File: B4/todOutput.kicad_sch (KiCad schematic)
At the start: 0 parts

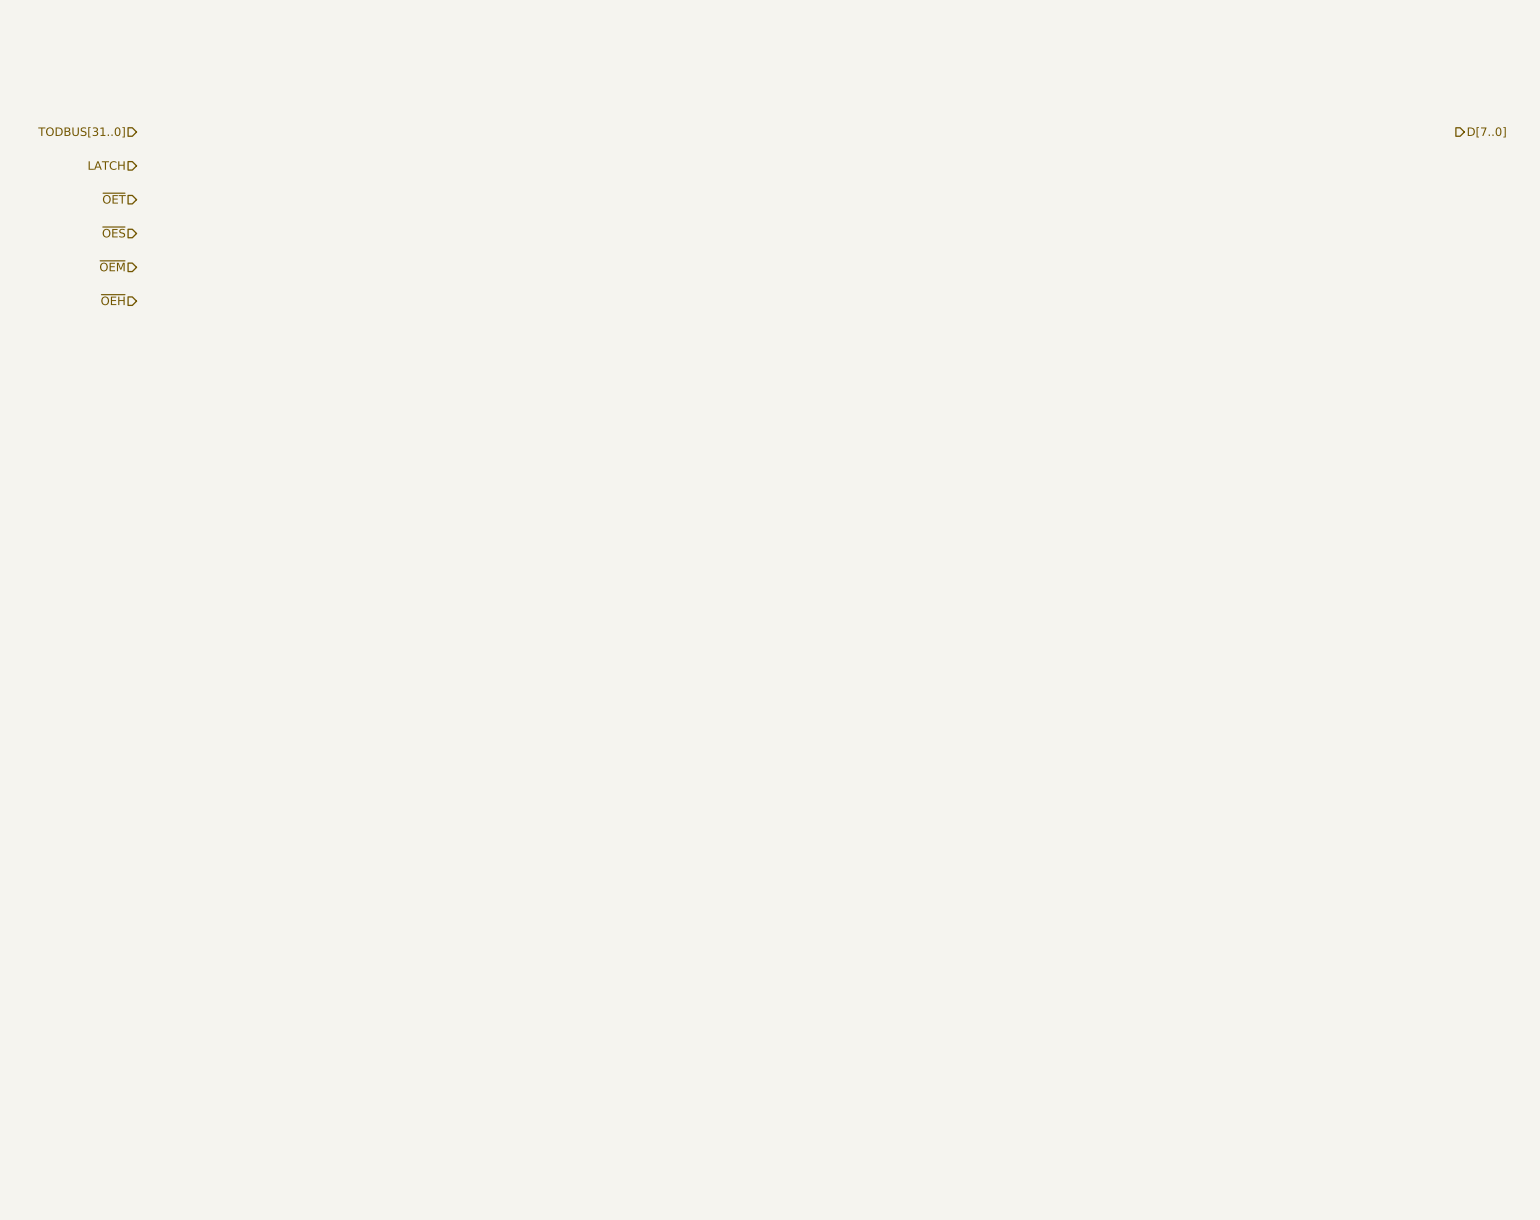
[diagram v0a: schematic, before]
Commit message: B2 refactored. B4 Added. TOD sch completed.
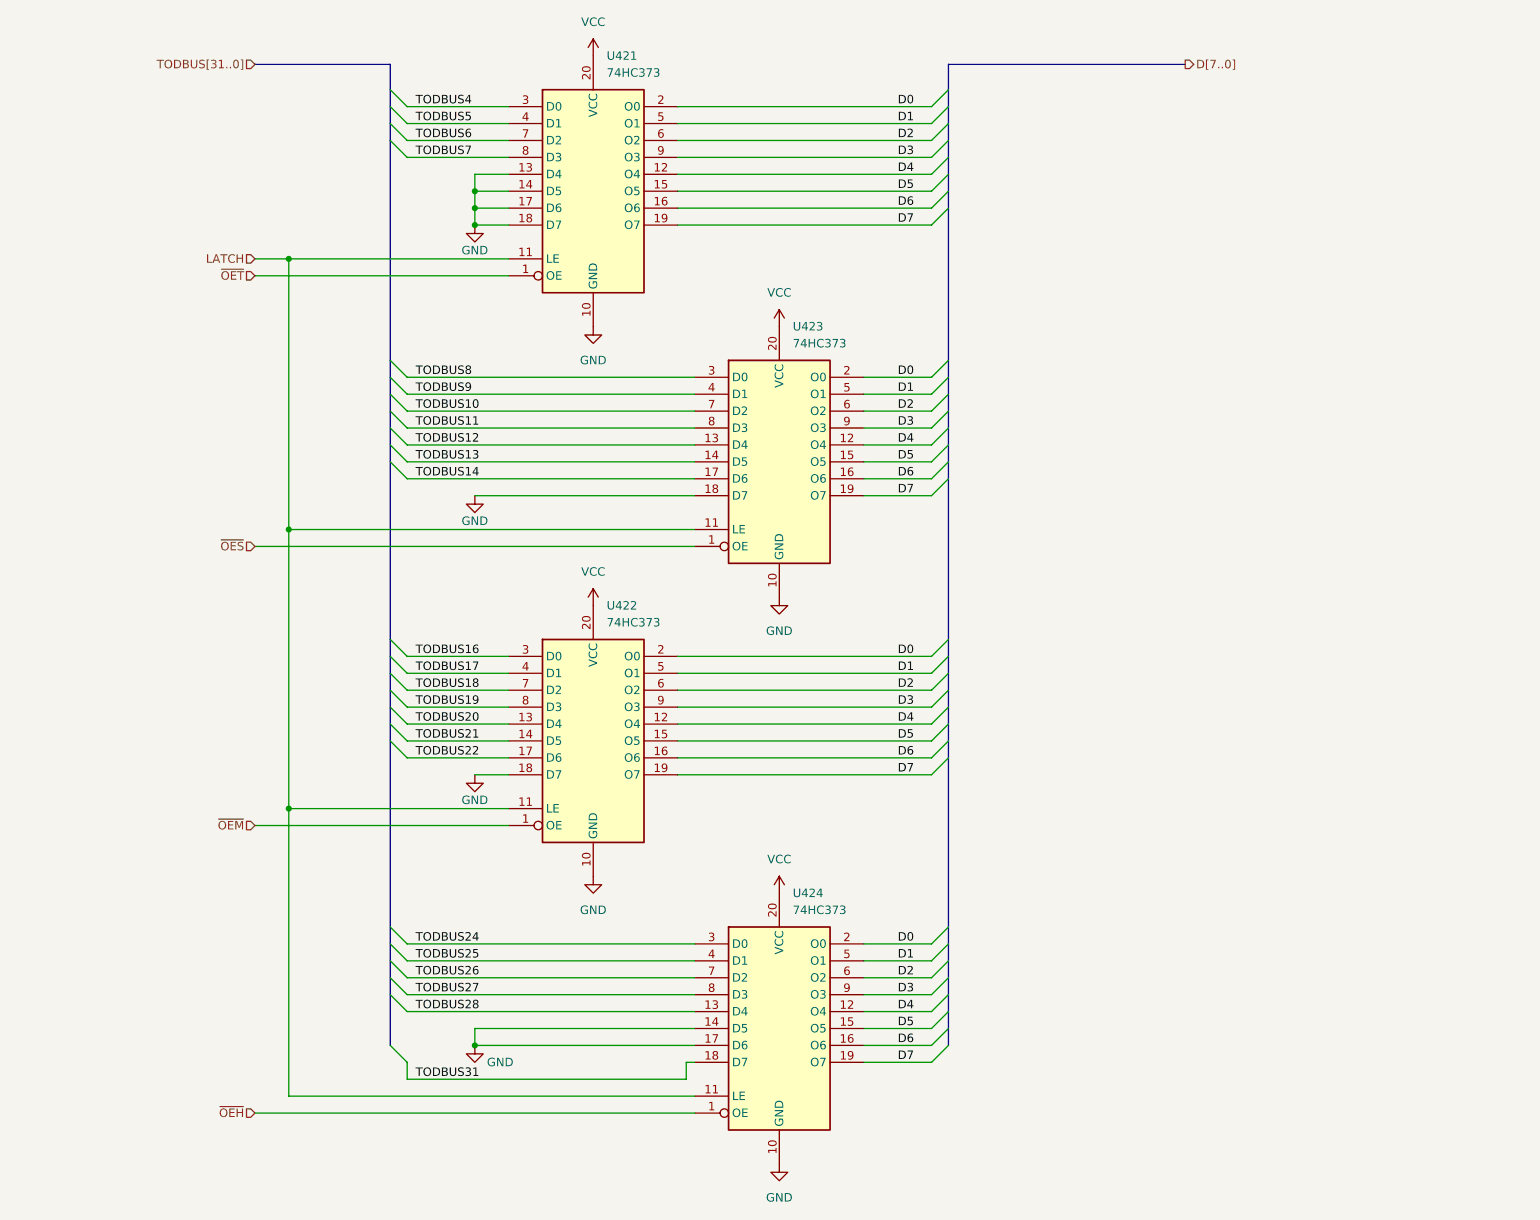
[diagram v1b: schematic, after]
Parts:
- added U421, U422, U423, U424: 74HC373, Package_SO:SOIC-20W_7.5x12.8mm_P1.27mm, symbol 74xx:74HC373
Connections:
- net LATCH: now also U421.11 (LE), U422.11 (LE), U423.11 (LE), U424.11 (LE)
- net ~{OEH}: now also U424.1 (OE)
- net ~{OEM}: now also U422.1 (OE)
- net ~{OES}: now also U423.1 (OE)
- net ~{OET}: now also U421.1 (OE)
- new net D0: U421.2 (O0), U422.2 (O0), U423.2 (O0), U424.2 (O0)
- new net D1: U421.5 (O1), U422.5 (O1), U423.5 (O1), U424.5 (O1)
- new net D2: U421.6 (O2), U422.6 (O2), U423.6 (O2), U424.6 (O2)
- new net D3: U421.9 (O3), U422.9 (O3), U423.9 (O3), U424.9 (O3)
- new net D4: U421.12 (O4), U422.12 (O4), U423.12 (O4), U424.12 (O4)
- new net D5: U421.15 (O5), U422.15 (O5), U423.15 (O5), U424.15 (O5)
- new net D6: U421.16 (O6), U422.16 (O6), U423.16 (O6), U424.16 (O6)
- new net D7: U421.19 (O7), U422.19 (O7), U423.19 (O7), U424.19 (O7)
- new net GND: U421.10 (GND), U421.13 (D4), U421.14 (D5), U421.17 (D6), U421.18 (D7), U422.10 (GND), U422.18 (D7), U423.10 (GND), U423.18 (D7), U424.10 (GND), U424.14 (D5), U424.17 (D6)
- new net TODBUS10: U423.7 (D2)
- new net TODBUS11: U423.8 (D3)
- new net TODBUS12: U423.13 (D4)
- new net TODBUS13: U423.14 (D5)
- new net TODBUS14: U423.17 (D6)
- new net TODBUS16: U422.3 (D0)
- new net TODBUS17: U422.4 (D1)
- new net TODBUS18: U422.7 (D2)
- new net TODBUS19: U422.8 (D3)
- new net TODBUS20: U422.13 (D4)
- new net TODBUS21: U422.14 (D5)
- new net TODBUS22: U422.17 (D6)
- new net TODBUS24: U424.3 (D0)
- new net TODBUS25: U424.4 (D1)
- new net TODBUS26: U424.7 (D2)
- new net TODBUS27: U424.8 (D3)
- new net TODBUS28: U424.13 (D4)
- new net TODBUS31: U424.18 (D7)
- new net TODBUS4: U421.3 (D0)
- new net TODBUS5: U421.4 (D1)
- new net TODBUS6: U421.7 (D2)
- new net TODBUS7: U421.8 (D3)
- new net TODBUS8: U423.3 (D0)
- new net TODBUS9: U423.4 (D1)
- new net VCC: U421.20 (VCC), U422.20 (VCC), U423.20 (VCC), U424.20 (VCC)

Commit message: TOD is here
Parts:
- renumbered U421 to U405
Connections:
- net D0: now also U405.5 (O1), U422.5 (O1), U423.5 (O1), U424.5 (O1); no longer U405.2 (O0), U422.2 (O0), U423.2 (O0), U424.2 (O0)
- net D1: now also U405.2 (O0), U422.2 (O0), U423.2 (O0), U424.2 (O0); no longer U405.5 (O1), U422.5 (O1), U423.5 (O1), U424.5 (O1)
- net D4: now also U405.15 (O5), U422.15 (O5), U423.15 (O5), U424.15 (O5); no longer U405.12 (O4), U422.12 (O4), U423.12 (O4), U424.12 (O4)
- net D5: now also U405.16 (O6), U422.16 (O6), U423.16 (O6), U424.16 (O6); no longer U405.15 (O5), U422.15 (O5), U423.15 (O5), U424.15 (O5)
- net D6: now also U405.12 (O4), U422.12 (O4), U423.12 (O4), U424.12 (O4); no longer U405.16 (O6), U422.16 (O6), U423.16 (O6), U424.16 (O6)
- net GND: now also U424.13 (D4); no longer U424.14 (D5)
- net TODBUS12: now also U423.14 (D5); no longer U423.13 (D4)
- net TODBUS13: now also U423.17 (D6); no longer U423.14 (D5)
- net TODBUS14: now also U423.13 (D4); no longer U423.17 (D6)
- net TODBUS16: now also U422.4 (D1); no longer U422.3 (D0)
- net TODBUS17: now also U422.3 (D0); no longer U422.4 (D1)
- net TODBUS20: now also U422.14 (D5); no longer U422.13 (D4)
- net TODBUS21: now also U422.17 (D6); no longer U422.14 (D5)
- net TODBUS22: now also U422.13 (D4); no longer U422.17 (D6)
- net TODBUS24: now also U424.4 (D1); no longer U424.3 (D0)
- net TODBUS25: now also U424.3 (D0); no longer U424.4 (D1)
- net TODBUS28: now also U424.14 (D5); no longer U424.13 (D4)
- net TODBUS4: now also U405.4 (D1); no longer U405.3 (D0)
- net TODBUS5: now also U405.3 (D0); no longer U405.4 (D1)
- net TODBUS8: now also U423.4 (D1); no longer U423.3 (D0)
- net TODBUS9: now also U423.3 (D0); no longer U423.4 (D1)

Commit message: Ready for v0.2.2
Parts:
- renumbered U405 to U406, U423 to U412, U422 to U417
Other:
- company: (none) -> Daniel Molina
- title: (none) -> 74HCT6526 Board 4
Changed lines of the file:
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@@
 (kicad_sch (version 20211123) (generator eeschema)
   (paper "A4")
+  (title_block
+    (title "74HCT6526 Board 4")
+    (date "2023-06-22")
+    (rev "0.2.2")
+    (company "Daniel Molina")
+    (comment 1 "https://github.com/dmolinagarcia/74HCT6526")
+  )
   (junction (at 104.14 39.37) (diameter 0) (color 0 0 0 0)
   )
@@
   (symbol (lib_id "74xx:74HC373") (at 149.86 80.01 0) (unit 1)
     (in_bom yes) (on_board yes) (fields_autoplaced)
-    (property "Reference" "U423" (id 0) (at 151.8794 59.69 0)
+    (property "Reference" "U412" (id 0) (at 151.8794 59.69 0)
       (effects (font (size 1.27 1.27)) (justify left))
     )
@@
   (symbol (lib_id "74xx:74HC373") (at 121.92 39.37 0) (unit 1)
     (in_bom yes) (on_board yes) (fields_autoplaced)
-    (property "Reference" "U405" (id 0) (at 123.9394 19.05 0)
+    (property "Reference" "U406" (id 0) (at 123.9394 19.05 0)
       (effects (font (size 1.27 1.27)) (justify left))
     )
@@
   (symbol (lib_id "74xx:74HC373") (at 121.92 121.92 0) (unit 1)
     (in_bom yes) (on_board yes) (fields_autoplaced)
-    (property "Reference" "U422" (id 0) (at 123.9394 101.6 0)
+    (property "Reference" "U417" (id 0) (at 123.9394 101.6 0)
       (effects (font (size 1.27 1.27)) (justify left))
     )
